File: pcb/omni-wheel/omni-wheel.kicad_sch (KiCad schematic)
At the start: 12 parts, among them J1 Motor1_input, J2 Motor2_input, J3 Motor4_input, J4 Motor3_input, J5 STLINK, J6 3.3V Input, J7 12V Input, U1 SN754410NE, U2 SN754410NE, U3 STM32F030R8Tx

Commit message: PCB save
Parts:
- added J8: 5V Input, symbol Connector_Generic:Conn_01x02
- added U4, U5: SN74HCT74DR, SN74HCT74DR:D14, symbol SN74HCT74DR:SN74HCT74DR
- added U6: SN74AC86DR, D14, symbol SN74AC86DR:SN74AC86DR
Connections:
- net GND: now also J8.2 (Pin_2)
- new net +5V: J8.1 (Pin_1)
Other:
- moved on the sheet: C1, C2, J5, J6, J7, U3

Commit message: pcb update for home
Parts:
- J6, J7, J8: footprint (none) -> Connector_AMASS:AMASS_XT60PW-M_1x02_P7.20mm_Horizontal
- U6: footprint D14 -> SN74AC86DR:D14
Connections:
- net +5V: now also U6.14 (VCC)
- net GND: now also U4.7 (GND), U6.7 (GND)
- net Motor1_ENCA: now also U6.1 (1A); no longer U3.10 (PC2)
- net Motor1_ENCB: now also U6.2 (1B); no longer U3.11 (PC3)
- net Motor2_ENCA: now also U6.4 (2A); no longer U3.37 (PC6)
- net Motor2_ENCB: now also U6.5 (2B); no longer U3.38 (PC7)
- net Motor3_ENCA: now also U6.9 (3A); no longer U3.51 (PC10)
- net Motor3_ENCB: now also U6.10 (3B); no longer U3.52 (PC11)
- net Motor4_ENCA: now also U6.12 (4A); no longer U3.3 (PC14)
- net Motor4_ENCB: now also U6.13 (4B); no longer U3.4 (PC15)
- net Motor4_EncTicks: now reaches U6.11 (4Y)
- net Motor4_EncTicks: now also U3.3 (PC14)
- net Motor1_EncTicks: now reaches U6.3 (1Y)
- net Motor1_EncTicks: now also U3.10 (PC2)
- net Motor2_EncTicks: now reaches U6.6 (2Y)
- net Motor2_EncTicks: now also U3.37 (PC6)
- net Motor3_EncTicks: now reaches U6.8 (3Y)
- net Motor3_EncTicks: now also U3.51 (PC10)
- net *1CLR: now reaches U4.1 (*1CLR)
- net 1D: now reaches U4.2 (1D)
- net 1CLK: now reaches U4.3 (1CLK)
- net *1PRE: now reaches U4.4 (*1PRE)
- net 1Q: now reaches U4.5 (1Q)
- net *1Q: now reaches U4.6 (*1Q)
- new net Motor1_Dir: U3.11 (PC3)
- new net Motor2_Dir: U3.38 (PC7)
- new net Motor3_Dir: U3.52 (PC11)
- new net Motor4_Dir: U3.4 (PC15)
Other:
- moved on the sheet: C1, C2, J1, J2, J3, J4, J5, J6, J7, J8, U1, U2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

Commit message: power distribution done, lay up  is next
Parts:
- removed J1: Motor1_input, symbol Connector:Conn_01x06_Pin
- removed J6: 3.3V Input, Connector_AMASS:AMASS_XT60PW-M_1x02_P7.20mm_Horizontal, symbol Connector_Generic:Conn_01x02
- removed J8: 5V Input, Connector_AMASS:AMASS_XT60PW-M_1x02_P7.20mm_Horizontal, symbol Connector_Generic:Conn_01x02
- removed U4, U5: SN74HCT74DR, SN74HCT74DR:D14, symbol SN74HCT74DR:SN74HCT74DR
- added C11: 10uF, Capacitor_SMD:C_0603_1608Metric, symbol Device:C
- added C12, C3: 100nF, Capacitor_SMD:C_0603_1608Metric, symbol Device:C
- added C4: 47pF, Capacitor_SMD:C_0603_1608Metric, symbol Device:C
- added C5, C6, C7, C8: 22uF, Capacitor_SMD:C_0603_1608Metric, symbol Device:C
- added C9: 56pF, Capacitor_SMD:C_0603_1608Metric, symbol Device:C
- added IC1, IC2: AP63301WU-7, SOT95P280X100-6N, symbol AP63301WU-7:AP63301WU-7
- added J6: Motor1_output, Connector_JST:JST_PH_B6B-PH-K_1x06_P2.00mm_Vertical, symbol Connector:Conn_01x06_Pin
- added L1: 6.8u, Inductor_SMD:L_0603_1608Metric, symbol Device:L
- added L2: 4.7u, Inductor_SMD:L_0603_1608Metric, symbol Device:L
- added R1: 158k, Resistor_SMD:R_0603_1608Metric, symbol Device:R
- added R2, R4: 30.1k, Resistor_SMD:R_0603_1608Metric, symbol Device:R
- added R3: 93.1k, Resistor_SMD:R_0603_1608Metric, symbol Device:R
- added U4: CD74HC04E, CD74HC04E:N14, symbol CD74HC04E:CD74HC04E
- C1: value .1uF -> .1 uF; footprint (none) -> Capacitor_SMD:C_0603_1608Metric; digikey# (none) -> 311-1088-2-ND; manf# (none) -> CC0603KRX7R7BB104
- C2: footprint (none) -> Capacitor_SMD:C_0603_1608Metric; digikey# (none) -> 311-1088-2-ND; manf# (none) -> CC0603KRX7R7BB104
- J2: value Motor2_input -> Motor2_output; footprint (none) -> Connector_JST:JST_PH_B6B-PH-K_1x06_P2.00mm_Vertical
- J3: value Motor4_input -> Motor4_output; footprint (none) -> Connector_JST:JST_PH_B6B-PH-K_1x06_P2.00mm_Vertical
- J4: value Motor3_input -> Motor3_output; footprint (none) -> Connector_JST:JST_PH_B6B-PH-K_1x06_P2.00mm_Vertical
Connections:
- net +12V: now also C11.1, IC1.2 (EN), IC1.3 (VIN), IC2.2 (EN), IC2.3 (VIN)
- net +3.3V: now also C7.2, C9.1, J6.5 (Pin_5), L2.1, R3.1
- net +5V: now also C4.1, C5.2, L1.1, R1.1, U4.14 (VCC)
- net GND: now also C11.2, C6.1, C8.1, J6.2 (Pin_2), R2.2, R4.2, U4.7 (GND)
- net Motor1_1A: now also U4.1 (1A)
- net Motor1_2A: now also U4.2 (*1Y); no longer U3.9 (PC1)
- net Motor1_EN: now also U3.9 (PC1)
- net Motor1_ENCA: now also J6.3 (Pin_3)
- net Motor1_ENCB: now also J6.4 (Pin_4)
- net Motor1_M1: now also J6.1 (Pin_1)
- net Motor1_M2: now also J6.6 (Pin_6)
- net Motor2_3A: now also U4.3 (2A)
- net Motor2_4A: now also U4.4 (*2Y); no longer U3.25 (PC5)
- net Motor2_EN: now also U3.25 (PC5)
- net Motor3_1A: now also U4.5 (3A)
- net Motor3_2A: now also U4.6 (*3Y); no longer U3.40 (PC9)
- net Motor3_EN: now also U3.40 (PC9)
- net Motor4_3A: now also U4.9 (4A)
- net Motor4_4A: now also U4.8 (*4Y); no longer U3.2 (PC13)
- net Motor4_EN: now also U3.2 (PC13)
- net Motor1_Dir: no longer names the net of U3.11 (PC3)
- net Motor2_Dir: no longer names the net of U3.38 (PC7)
- net Motor3_Dir: no longer names the net of U3.52 (PC11)
- net Motor4_Dir: no longer names the net of U3.4 (PC15)
- new net: C9.2, IC2.1 (FB), R3.2, R4.1
- new net: C12.1, IC2.5 (SW)
- new net: C12.2, IC2.6 (BST)
- new net: C7.1, C8.2
- new net: C3.1, IC1.5 (SW), L1.2
- new net: C4.2, IC1.1 (FB), R1.2, R2.1
- new net: C3.2, IC1.6 (BST)
- new net: C5.1, C6.2
- no-connect marks 0 -> 4
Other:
- note added: "POWER DISTRIBUTION"
- moved on the sheet: J7, U6

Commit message: pcb update for home
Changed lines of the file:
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@@
+	)
+	(symbol
+		(lib_id "power:GND")
+		(at 66.04 161.29 0)
+		(unit 1)
+		(exclude_from_sim no)
+		(in_bom yes)
+		(on_board yes)
+		(dnp no)
+		(fields_autoplaced yes)
+		(property "Reference" "#PWR01"
+			(at 66.04 167.64 0)
+			(effects
+				(font
+					(size 1.27 1.27)
+				)
+				(hide yes)
+			)
+		)
+		(property "Value" "GND"
+			(at 66.04 166.37 0)
+			(effects
+				(font
+					(size 1.27 1.27)
+				)
+			)
+		)
+		(property "Footprint" ""
+			(at 66.04 161.29 0)
+			(effects
+				(font
+					(size 1.27 1.27)
+				)
+				(hide yes)
+			)
+		)
+		(property "Datasheet" ""
+			(at 66.04 161.29 0)
+			(effects
+				(font
+					(size 1.27 1.27)
+				)
+				(hide yes)
+			)
+		)
+		(property "Description" "Power symbol creates a global label with name \"GND\" , ground"
+			(at 66.04 161.29 0)
+			(effects
+				(font
+					(size 1.27 1.27)
+				)
+				(hide yes)
+			)
+		)
+		(pin "1"
+		)
+		(instances
+			(project "omni-wheel"
+				(path "/00bcea37-6431-4bf6-91e9-3738f9d2ffd8"
+					(reference "#PWR01")
+					(unit 1)
+				)
+			)
+		)
 	)
 	(symbol

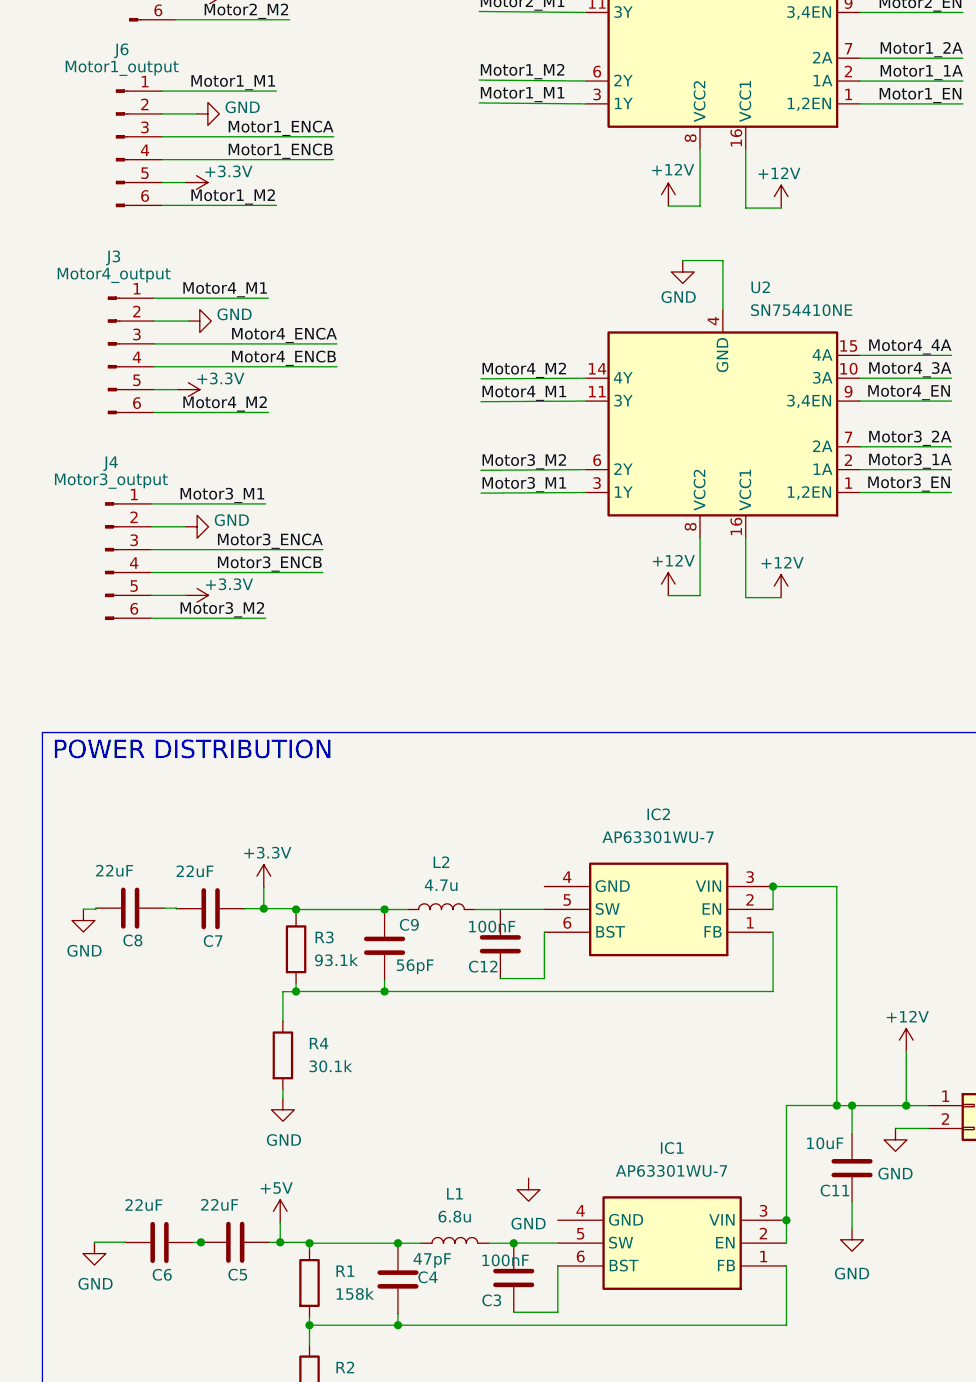
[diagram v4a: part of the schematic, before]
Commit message: routing almost done, need to logic pins next
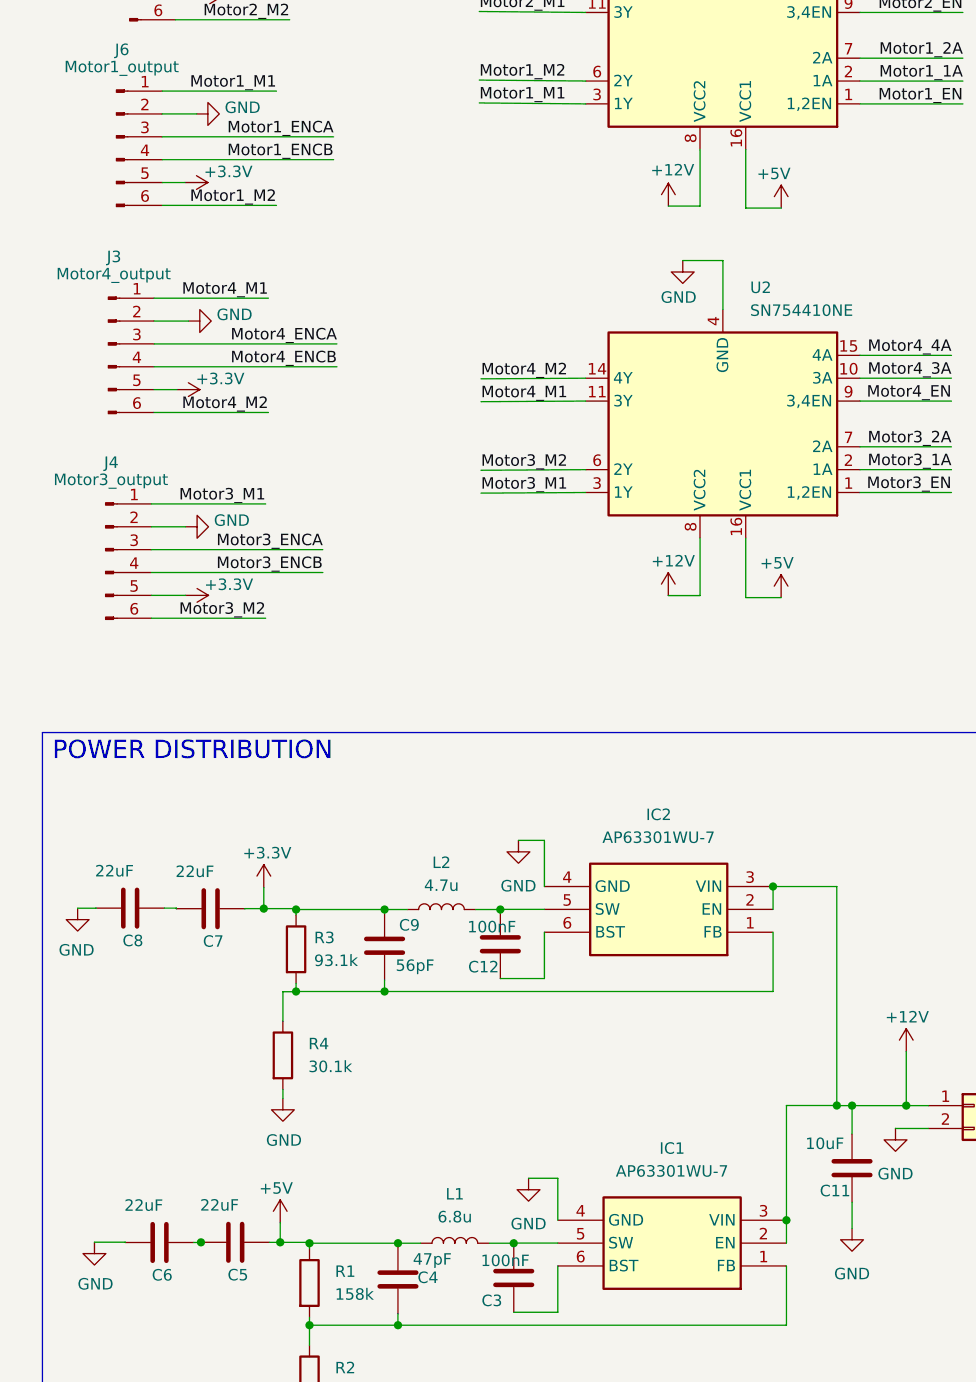
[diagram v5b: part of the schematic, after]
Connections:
- net +12V: no longer U1.16 (VCC1), U2.16 (VCC1)
- net +5V: now also U1.16 (VCC1), U2.16 (VCC1)
- net GND: now also IC1.4 (GND), IC2.4 (GND)
- net at C12.1, IC2.5 (SW): now also L2.2
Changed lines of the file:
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@@
 	)
 	(junction
+		(at 62.9052 131.424)
+		(diameter 0)
+		(color 0 0 0 0)
+	)
+	(junction
 		(at 108.0081 153.2124)
 		(diameter 0)
@@
 	(wire
 		(pts
+			(xy 62.9052 131.424) (xy 62.9052 131.474)
+		)
+		(stroke
+			(width 0)
+			(type default)
+		)
+	)
+	(wire
+		(pts
 			(xy 263.7566 96.0537) (xy 271.3766 96.0537)
 		)
@@
 	(wire
 		(pts
+			(xy 67.8024 128.87) (xy 67.8024 123.7454)
+		)
+		(stroke
+			(width 0)
+			(type default)
+		)
+	)
+	(wire
+		(pts
+			(xy 67.8024 123.7454) (xy 64.9177 123.7454)
+		)
+		(stroke
+			(width 0)
+			(type default)
+		)
+	)
+	(wire
+		(pts
 			(xy 127.0123 29.407) (xy 143.5223 29.407)
 		)
@@
 	(wire
 		(pts
-			(xy 17.9664 131.3814) (xy 17.9664 131.2701)
-		)
-		(stroke
-			(width 0)
-			(type default)
-		)
-	)
-	(wire
-		(pts
 			(xy 67.8024 131.41) (xy 62.9052 131.41)
 		)
@@
 	(wire
 		(pts
-			(xy 60.1738 131.424) (xy 62.9052 131.424)
+			(xy 60.7522 74.9986) (xy 72.39 74.93)
 		)
 		(stroke
@@
 	(wire
 		(pts
-			(xy 60.7522 74.9986) (xy 72.39 74.93)
+			(xy 234.95 60.96) (xy 234.95 52.8737)
 		)
 		(stroke
@@
 	(wire
 		(pts
-			(xy 234.95 60.96) (xy 234.95 52.8737)
+			(xy 40.2086 139.6534) (xy 40.2086 140.532)
 		)
 		(stroke
@@
 	(wire
 		(pts
-			(xy 40.2086 139.6534) (xy 40.2086 140.532)
+			(xy 66.04 161.29) (xy 69.2919 161.29)
 		)
 		(stroke
@@
 	(wire
 		(pts
-			(xy 16.5812 131.3814) (xy 17.9664 131.3814)
-		)
-		(stroke
-			(width 0)
-			(type default)
-		)
-	)
-	(wire
-		(pts
 			(xy 113.03 69.85) (xy 102.87 69.85)
 		)
@@
 	(wire
 		(pts
+			(xy 17.9664 131.2784) (xy 17.9664 131.2701)
+		)
+		(stroke
+			(width 0)
+			(type default)
+		)
+	)
+	(wire
+		(pts
 			(xy 114.3 26.67) (xy 102.87 26.67)
 		)
@@
 	(wire
 		(pts
-			(xy 62.9052 131.41) (xy 62.9052 131.474)
+			(xy 69.2919 161.29) (xy 69.2919 165.9498)
 		)
 		(stroke
@@
 	(wire
 		(pts
+			(xy 15.9403 131.2784) (xy 17.9664 131.2784)
+		)
+		(stroke
+			(width 0)
+			(type default)
+		)
+	)
+	(wire
+		(pts
+			(xy 60.1738 131.424) (xy 62.9052 131.424)
+		)
+		(stroke
+			(width 0)
+			(type default)
+		)
+	)
+	(wire
+		(pts
 			(xy 26.8028 24.9415) (xy 45.8528 24.9415)
 		)
@@
 	(wire
 		(pts
+			(xy 62.9052 131.41) (xy 62.9052 131.424)
+		)
+		(stroke
+			(width 0)
+			(type default)
+		)
+	)
+	(wire
+		(pts
 			(xy 199.4023 26.867) (xy 201.9423 26.867)
 		)
@@
 			)
 		)
-		(property "Value" "+12V"
+		(property "Value" "+5V"
 			(at 91.3995 49.6806 0)
 			(effects
@@
 			)
 		)
-		(property "Value" "+12V"
+		(property "Value" "+5V"
 			(at 91.7499 92.9462 0)
 			(effects
@@
 	)
 	(symbol
+		(lib_id "power:GND")
+		(at 64.9177 123.7454 0)
+		(unit 1)
+		(exclude_from_sim no)
+		(in_bom yes)
+		(on_board yes)
+		(dnp no)
+		(property "Reference" "#PWR02"
+			(at 64.9177 130.0954 0)
+			(effects
+				(font
+					(size 1.27 1.27)
+				)
+				(hide yes)
+			)
+		)
+		(property "Value" "GND"
+			(at 64.9177 128.8254 0)
+			(effects
+				(font
+					(size 1.27 1.27)
+				)
+			)
+		)
+		(property "Footprint" ""
+			(at 64.9177 123.7454 0)
+			(effects
+				(font
+					(size 1.27 1.27)
+				)
+				(hide yes)
+			)
+		)
+		(property "Datasheet" ""
+			(at 64.9177 123.7454 0)
+			(effects
+				(font
+					(size 1.27 1.27)
+				)
+				(hide yes)
+			)
+		)
+		(property "Description" "Power symbol creates a global label with name \"GND\" , ground"
+			(at 64.9177 123.7454 0)
+			(effects
+				(font
+					(size 1.27 1.27)
+				)
+				(hide yes)
+			)
+		)
+		(pin "1"
+		)
+		(instances
+			(project "omni-wheel"
+				(path "/00bcea37-6431-4bf6-91e9-3738f9d2ffd8"
+					(reference "#PWR02")
+					(unit 1)
+				)
+			)
+		)
+	)
+	(symbol
 		(lib_id "power:+3.3V")
 		(at 26.9735 73.6576 270)
@@
 	(symbol
 		(lib_id "power:GND")
-		(at 16.5812 131.3814 0)
+		(at 15.9403 131.2784 0)
+		(mirror y)
 		(unit 1)
 		(exclude_from_sim no)
@@
 		(dnp no)
 		(property "Reference" "#PWR032"
-			(at 16.5812 137.7314 0)
+			(at 15.9403 137.6284 0)
 			(effects
 				(font
@@
 		)
 		(property "Value" "GND"
-			(at 18.6972 136.0543 0)
+			(at 13.8243 135.9513 0)
 			(effects
 				(font
@@
 		)
 		(property "Footprint" ""
-			(at 16.5812 131.3814 0)
+			(at 15.9403 131.2784 0)
 			(effects
 				(font
@@
 		)
 		(property "Datasheet" ""
-			(at 16.5812 131.3814 0)
+			(at 15.9403 131.2784 0)
 			(effects
 				(font
@@
 		)
 		(property "Description" "Power symbol creates a global label with name \"GND\" , ground"
-			(at 16.5812 131.3814 0)
+			(at 15.9403 131.2784 0)
 			(effects
 				(font

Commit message: save before architecture change
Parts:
- added C10, C13, C14, C15, C16, C17: .1 uF, Capacitor_SMD:C_0603_1608Metric, symbol Device:C
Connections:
- net +12V: now also C10.1, C15.1
- net +5V: now also C13.1, C14.1, C16.1, C17.1
- net GND: now also C10.2, C13.2, C14.2, C15.2, C16.2, C17.2
- net Motor1_1A: now also U3.11 (PC3), U4.5 (3A); no longer U3.8 (PC0), U4.1 (1A)
- net Motor1_2A: now also U4.6 (*3Y); no longer U4.2 (*1Y)
- net Motor1_EN: now also U3.50 (PA15); no longer U3.16 (PA2), U3.9 (PC1)
- net Motor1_ENCA: now also U6.4 (2A); no longer U6.1 (1A)
- net Motor1_ENCB: now also U6.5 (2B); no longer U6.2 (1B)
- net Motor1_EncTicks: now also U3.38 (PC7), U6.6 (2Y); no longer U3.10 (PC2), U6.3 (1Y)
- net Motor2_3A: now also U3.10 (PC2); no longer U3.24 (PC4)
- net Motor2_EN: now also U3.51 (PC10); no longer U3.20 (PA4), U3.25 (PC5)
- net Motor2_ENCA: now also U6.1 (1A); no longer U6.4 (2A)
- net Motor2_ENCB: now also U6.2 (1B); no longer U6.5 (2B)
- net Motor2_EncTicks: now also U6.3 (1Y); no longer U6.6 (2Y)
- net Motor3_1A: now also U3.9 (PC1), U4.11 (5A); no longer U3.39 (PC8), U4.5 (3A)
- net Motor3_2A: now also U4.10 (*5Y); no longer U4.6 (*3Y)
- net Motor3_EN: now also U3.52 (PC11); no longer U3.22 (PA6), U3.40 (PC9)
- net Motor3_ENCA: now also U6.12 (4A); no longer U6.9 (3A)
- net Motor3_ENCB: now also U6.13 (4B); no longer U6.10 (3B)
- net Motor3_EncTicks: now also U3.40 (PC9), U6.11 (4Y); no longer U3.51 (PC10), U6.8 (3Y)
- net Motor4_3A: now also U3.8 (PC0); no longer U3.53 (PC12)
- net Motor4_EN: now also U3.53 (PC12); no longer U3.2 (PC13), U3.23 (PA7)
- net Motor4_ENCA: now also U6.9 (3A); no longer U6.12 (4A)
- net Motor4_ENCB: now also U6.10 (3B); no longer U6.13 (4B)
- net Motor4_EncTicks: now also U3.39 (PC8), U6.8 (3Y); no longer U3.3 (PC14), U6.11 (4Y)
- no-connect marks 4 -> 34
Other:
- moved on the sheet: R4

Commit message: first pcb revision done
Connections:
- net Motor1_EN: now also U3.20 (PA4); no longer U3.50 (PA15)
- net Motor2_EN: now also U3.16 (PA2); no longer U3.51 (PC10)
- net Motor3_EN: now also U3.23 (PA7); no longer U3.52 (PC11)
- net Motor4_EN: now also U3.22 (PA6); no longer U3.53 (PC12)
- no-connect marks 34 -> 45
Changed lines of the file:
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@@
+	)
+	(no_connect
+		(at 217.17 81.28)
+	)
+	(no_connect
+		(at 217.17 78.74)
 	)
 	(no_connect
@@
 	)
 	(no_connect
+		(at 217.17 137.16)
+	)
+	(no_connect
+		(at 217.17 134.62)
+	)
+	(no_connect
 		(at 247.65 111.76)
 	)
@@
 	)
 	(no_connect
-		(at 247.65 81.28)
-	)
-	(no_connect
-		(at 247.65 71.12)
-	)
-	(no_connect
-		(at 247.65 83.82)
+		(at 217.17 124.46)
+	)
+	(no_connect
+		(at 217.17 111.76)
+	)
+	(no_connect
+		(at 217.17 109.22)
+	)
+	(no_connect
+		(at 217.17 76.2)
+	)
+	(no_connect
+		(at 217.17 93.98)
+	)
+	(no_connect
+		(at 217.17 83.82)
+	)
+	(no_connect
+		(at 217.17 129.54)
 	)
 	(no_connect
@@
 	)
 	(no_connect
+		(at 217.17 127)
+	)
+	(no_connect
 		(at 247.65 127)
 	)
@@
 	)
 	(no_connect
-		(at 247.65 76.2)
+		(at 217.17 86.36)
+	)
+	(no_connect
+		(at 217.17 132.08)
 	)
 	(no_connect
@@
 		(at 247.65 68.58)
 	)
+	(no_connect
+		(at 217.17 88.9)
+	)
 	(wire
 		(pts
@@
 	(wire
 		(pts
-			(xy 199.39 129.54) (xy 217.17 129.54)
-		)
-		(stroke
-			(width 0)
-			(type default)
-		)
-	)
-	(wire
-		(pts
 			(xy 127.0123 31.947) (xy 143.5223 31.947)
 		)
@@
 	(wire
 		(pts
+			(xy 260.35 81.28) (xy 247.65 81.28)
+		)
+		(stroke
+			(width 0)
+			(type default)
+		)
+	)
+	(wire
+		(pts
 			(xy 106.8114 155.7524) (xy 106.8114 155.7504)
 		)
@@
 	(wire
 		(pts
-			(xy 199.39 124.46) (xy 217.17 124.46)
-		)
-		(stroke
-			(width 0)
-			(type default)
-		)
-	)
-	(wire
-		(pts
 			(xy 93.2024 140.532) (xy 50.0414 140.532)
 		)
@@
 	(wire
 		(pts
-			(xy 261.62 104.14) (xy 247.65 104.14)
-		)
-		(stroke
-			(width 0)
-			(type default)
-		)
-	)
-	(wire
-		(pts
 			(xy 207.3005 76.2124) (xy 195.8705 76.2124)
 		)
@@
 	(wire
 		(pts
-			(xy 199.39 127) (xy 217.17 127)
-		)
-		(stroke
-			(width 0)
-			(type default)
-		)
-	)
-	(wire
-		(pts
 			(xy 38.4497 166.227) (xy 38.4497 168.4025)
 		)
@@
 	(wire
 		(pts
+			(xy 260.35 71.12) (xy 247.65 71.12)
+		)
+		(stroke
+			(width 0)
+			(type default)
+		)
+	)
+	(wire
+		(pts
 			(xy 85.09 50.1004) (xy 85.09 46.99)
 		)
@@
 	(wire
 		(pts
+			(xy 260.35 76.2) (xy 247.65 76.2)
+		)
+		(stroke
+			(width 0)
+			(type default)
+		)
+	)
+	(wire
+		(pts
 			(xy 232.41 158.75) (xy 232.41 154.94)
 		)
@@
 		(pts
 			(xy 83.6034 16.0378) (xy 87.63 16.0378)
+		)
+		(stroke
+			(width 0)
+			(type default)
+		)
+	)
+	(wire
+		(pts
+			(xy 260.35 83.82) (xy 247.65 83.82)
 		)
 		(stroke
@@
 		)
 	)
+	(label "Motor2_EN"
+		(at 260.35 71.12 180)
+		(fields_autoplaced yes)
+		(effects
+			(font
+				(size 1.27 1.27)
+			)
+			(justify right bottom)
+		)
+	)
 	(label "Motor2_M2"
 		(at 60.5625 29.105 0)
@@
 		)
 	)
-	(label "Motor2_EN"
-		(at 199.39 124.46 0)
-		(fields_autoplaced yes)
-		(effects
-			(font
-				(size 1.27 1.27)
-			)
-			(justify left bottom)
-		)
-	)
 	(label "Motor4_3A"
 		(at 113.03 72.39 180)
@@
 		)
 	)
-	(label "Motor1_EN"
-		(at 261.62 104.14 180)
-		(fields_autoplaced yes)
-		(effects
-			(font
-				(size 1.27 1.27)
-			)
-			(justify right bottom)
-		)
-	)
 	(label "Motor4_4A"
 		(at 113.03 69.85 180)
@@
 		)
 	)
+	(label "Motor3_EN"
+		(at 260.35 83.82 180)
+		(fields_autoplaced yes)
+		(effects
+			(font
+				(size 1.27 1.27)
+			)
+			(justify right bottom)
+		)
+	)
 	(label "Motor2_ENCA"
 		(at 45.8528 24.9415 180)
@@
 		)
 	)
-	(label "Motor4_EN"
-		(at 199.39 129.54 0)
-		(fields_autoplaced yes)
-		(effects
-			(font
-				(size 1.27 1.27)
-			)
-			(justify left bottom)
-		)
-	)
 	(label "Motor3_M1"
 		(at 60.7522 85.1586 0)
@@
 		)
 	)
-	(label "Motor3_EN"
-		(at 199.39 127 0)
-		(fields_autoplaced yes)
-		(effects
-			(font
-				(size 1.27 1.27)
-			)
-			(justify left bottom)
+	(label "Motor1_EN"
+		(at 260.35 76.2 180)
+		(fields_autoplaced yes)
+		(effects
+			(font
+				(size 1.27 1.27)
+			)
+			(justify right bottom)
 		)
 	)
@@
 		)
 	)
+	(label "Motor4_EN"
+		(at 260.35 81.28 180)
+		(fields_autoplaced yes)
+		(effects
+			(font
+				(size 1.27 1.27)
+			)
+			(justify right bottom)
+		)
+	)
